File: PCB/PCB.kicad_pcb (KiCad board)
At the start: 2 copper layers, 31 parts, among them SW1 Bourns PEC11R, SW2 Bourns PEC11R, U1 RPi_Pico_TH, U2 RDA5807M_Module, U3 LM386, U4 AP63205WU-7

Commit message: PCB design #1
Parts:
- added ?: , , F.Cu at (179.0, 53.5)
- added LS1: Speaker, 2pin_ScrewTerminal:691137710002, F.Cu at (177.5, 76.5)
- added SW3: SW_DPST, 2pin_ScrewTerminal:691137710002, F.Cu at (156.5, 131.0)
- added SW4: SW_DPST, 2pin_ScrewTerminal:691137710002, F.Cu at (145.5, 131.0)
- added SW5: SW_DPST, 2pin_ScrewTerminal:691137710002, F.Cu at (134.5, 131.0)
- BT1: footprint Battery:BatteryHolder_Bulgin_BX0034_1xAAA -> Battery:THT Battery Connection
- SW1, SW2: footprint Rotary_Encoder:RotaryEncoder_Alps_EC12E-Switch_Vertical_H20mm -> 5pin_ScrewTerminal:PHOENIX_1935190
- moved U3 100.2 mm to (158.0, 79.0)
- moved R3 88.6 mm to (172.2, 84.0)
- moved U2 84.9 mm to (171.4, 63.5)
- moved BT1 78.1 mm to (128.2, 65.9)
- moved C1 72.4 mm to (164.5, 84.0)
- moved C2 70.0 mm to (164.5, 77.5)
- moved U1 69.9 mm to (141.1, 97.4)
- moved C10 69.9 mm to (131.2, 59.9)
- moved C11 69.9 mm to (131.2, 57.4)
- moved C8 69.9 mm to (132.8, 66.9)
- moved C9 69.9 mm to (135.8, 60.4)
- moved U4 69.9 mm to (133.2, 63.5)
- moved L1 69.9 mm to (137.4, 63.4)
- moved R2 68.2 mm to (152.7, 64.5)
- moved R1 68.1 mm to (152.7, 61.5)
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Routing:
- net /Encoder2SW: track 0.00 -> 66.0 mm
- net /B1: track 0.00 -> 46.7 mm
- net /Encoder2B: track 0.00 -> 42.6 mm
- net Net-(U1-VSYS): track 43.1 -> 0.61 mm
- net /Radio sdio: track 0.00 -> 41.1 mm
- net /Radio sclk: track 0.00 -> 40.9 mm
- net /B2: track 0.00 -> 39.3 mm
- net /Display CS: track 0.00 -> 37.1 mm
- net /Encoder1SW: track 0.00 -> 35.4 mm
- net /B3: track 0.00 -> 34.7 mm
- net Net-(U2-LOUT): track 0.00 -> 31.9 mm
- net /Encoder1A: track 0.00 -> 31.9 mm
- net /Display res: track 0.00 -> 25.8 mm
- net /Encoder2A: track 0.00 -> 23.5 mm
- net Net-(R4-Pad2): track 0.00 -> 21.4 mm
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- added copper zone on F.Cu, net 3V3
- added copper zone on B.Cu, net GND
- added copper zone on F.Cu, net GND
- added copper zone on F.Cu, net Net-(BT1-+)
- added copper zone on F.Cu, net Net-(U1-VSYS)
- added copper zone on F.Cu, net Net-(U4-SW)
- removed copper zone on F.Cu, net (none)
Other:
- board outline added: 83 x 95 mm

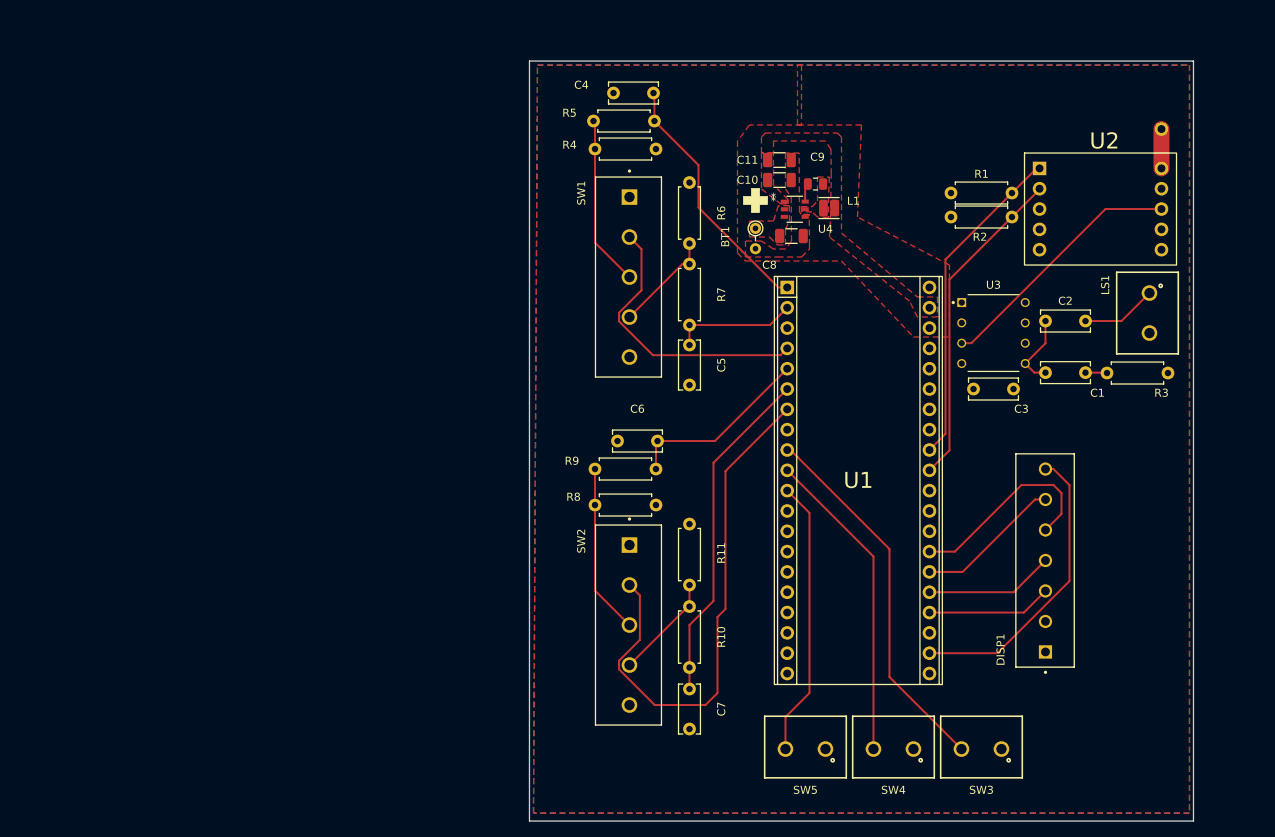
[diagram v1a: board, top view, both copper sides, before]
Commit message: Updated PCB
PCB updated to reflect new footprints and corrected connections.
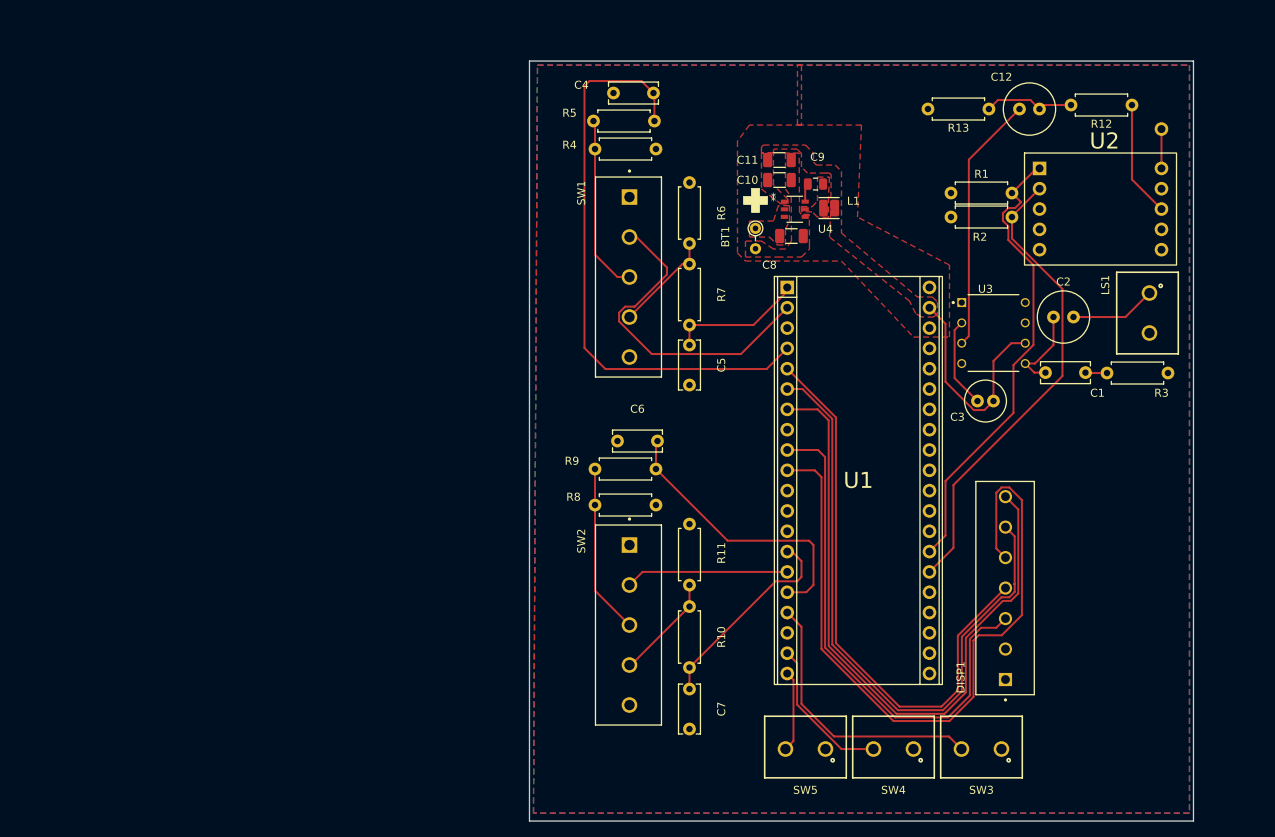
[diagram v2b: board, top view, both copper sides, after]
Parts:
- added C12: 470uF, Capacitor_THT:C_Radial_D6.3mm_H11.0mm_P2.50mm, F.Cu at (163.8, 51.0)
- added R12: 1k, Resistor_THT:R_Axial_DIN0207_L6.3mm_D2.5mm_P7.62mm_Horizontal, F.Cu at (175.3, 50.5)
- added R13: 150, Resistor_THT:R_Axial_DIN0207_L6.3mm_D2.5mm_P7.62mm_Horizontal, F.Cu at (157.4, 51.0)
- C2: footprint Capacitor_THT:C_Disc_D6.0mm_W2.5mm_P5.00mm -> Capacitor_THT:C_Radial_D6.3mm_H11.0mm_P2.50mm
- C3: value 470uF -> 10uF; footprint Capacitor_THT:C_Disc_D6.0mm_W2.5mm_P5.00mm -> Capacitor_THT:C_Radial_D5.0mm_H11.0mm_P2.00mm
- R3: value 10k -> 10
- moved DISP1 6.07 mm to (163.1, 124.2)
- moved C3 1.58 mm to (156.0, 87.5)
- moved C2 1.12 mm to (165.5, 77.0)
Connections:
- C10 pad 2: Net-(U1-VSYS) -> 5V
- C11 pad 2: Net-(U1-VSYS) -> 5V
- C3 pad 1: GND -> Net-(U3--)
- C3 pad 2: 3V3 -> 5V
- L1 pad 2: Net-(U1-VSYS) -> 5V
- SW1 pad C: unconnected-(SW1-PadC) -> GND
- SW2 pad C: unconnected-(SW2-PadC) -> GND
- U1 pad 1: /Encoder1A -> /Encoder1B
- U1 pad 10: /B2 -> /Display res
- U1 pad 11: /B3 -> unconnected-(U1-GP8-Pad11)
- U1 pad 14: unconnected-(U1-GP10-Pad14) -> /Encoder2B
- U1 pad 15: unconnected-(U1-GP11-Pad15) -> /Encoder2SW
- U1 pad 16: unconnected-(U1-GP12-Pad16) -> /Encoder2A
- U1 pad 17: unconnected-(U1-GP13-Pad17) -> /B1
- U1 pad 19: unconnected-(U1-GP14-Pad19) -> /B2
- U1 pad 2: /Encoder1B -> /Encoder1SW
- U1 pad 20: unconnected-(U1-GP15-Pad20) -> /B3
- U1 pad 22: /Display CS -> unconnected-(U1-GP17-Pad22)
- U1 pad 24: /Display sck -> unconnected-(U1-GP18-Pad24)
- U1 pad 25: /Display sda -> unconnected-(U1-GP19-Pad25)
- U1 pad 26: /Display DC -> /Radio sclk
- U1 pad 27: /Display res -> /Radio sdio
- U1 pad 31: /Radio sclk -> unconnected-(U1-GP26/ADC0-Pad31)
- U1 pad 32: /Radio sdio -> unconnected-(U1-GP27/ADC1-Pad32)
- U1 pad 39: Net-(U1-VSYS) -> 5V
- U1 pad 4: /Encoder1SW -> /Encoder1A
- U1 pad 5: /Encoder2A -> /Display sda
- U1 pad 6: /Encoder2B -> /Display DC
- U1 pad 7: /Encoder2SW -> /Display CS
- U1 pad 9: /B1 -> /Display sck
- U3 pad 2: GND -> Net-(U3--)
- U3 pad 3: Net-(U2-LOUT) -> Net-(U3-+)
- U3 pad 6: 3V3 -> 5V
- U4 pad 1: Net-(U1-VSYS) -> 5V
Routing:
- net /Display res: track 25.8 -> 91.6 mm
- net /Display DC: track 18.2 -> 80.3 mm
- net /Display sda: track 16.1 -> 71.4 mm
- net /Display sck: track 15.6 -> 64.3 mm
- net /Display CS: track 37.1 -> 84.2 mm
- net /Encoder2SW: track 66.0 -> 20.4 mm
- net /Encoder1A: track 31.9 -> 73.3 mm
- net Net-(U3-+): track 0.00 -> 32.3 mm
- net 5V: track 0.00 -> 27.9 mm
- net /B3: track 34.7 -> 10.2 mm
- net /B2: track 39.3 -> 18.8 mm
- net /Radio sclk: track 40.9 -> 58.8 mm
- net Net-(U2-LOUT): track 31.9 -> 14.5 mm
- net /Radio sdio: track 41.1 -> 58.4 mm
- net /Encoder2B: track 42.6 -> 25.6 mm
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- added copper zone on F.Cu, net 5V
- removed copper zone on F.Cu, net Net-(U1-VSYS)

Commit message: Updated PCB
PCB updated to have mounting holes, proper shape, etc.
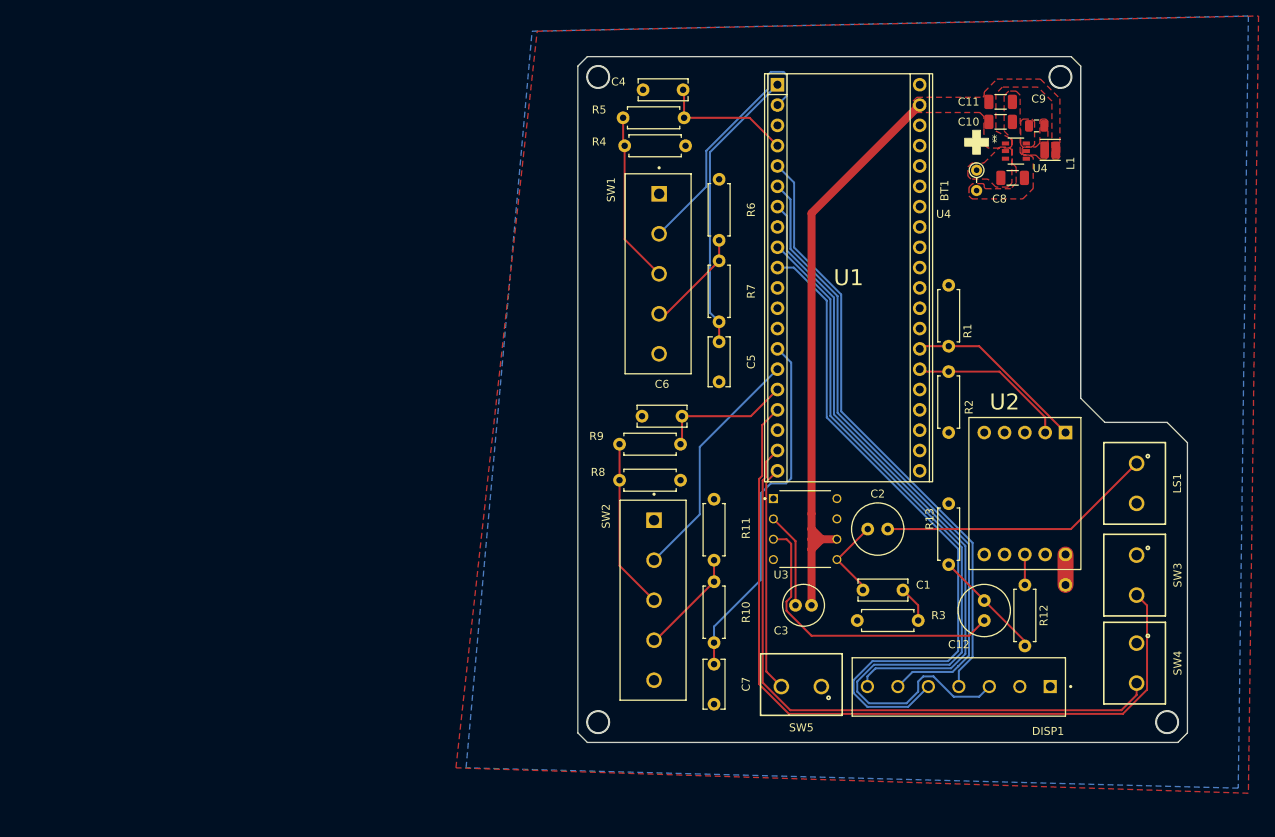
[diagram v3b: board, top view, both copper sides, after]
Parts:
- moved C12 61.8 mm to (156.8, 112.4), turned to -90 degrees
- moved R12 61.5 mm to (161.9, 110.5), turned to -90 degrees
- moved ? 58.2 mm to (167.0, 110.5)
- moved R13 57.2 mm to (152.4, 108.0), turned to 90 degrees
- moved R3 38.9 mm to (148.6, 114.9), turned to 180 degrees
- moved U2 36.8 mm to (161.9, 99.1), turned to -90 degrees
- moved C1 35.5 mm to (141.7, 111.1)
- moved C2 35.2 mm to (142.3, 103.5)
- moved C3 34.2 mm to (133.3, 113.0)
- moved U3 34.0 mm to (134.5, 103.5)
- moved SW4 32.2 mm to (175.9, 120.3), turned to -90 degrees
- moved SW3 29.1 mm to (175.9, 109.3), turned to -90 degrees
- moved BT1 28.6 mm to (155.9, 58.6)
- moved C10 28.6 mm to (158.9, 52.6)
- moved C11 28.6 mm to (158.9, 50.1)
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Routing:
- net /B1: track 35.3 -> 98.9 mm
- net /B2: track 18.8 -> 80.2 mm
- net /Encoder1A: track 73.3 -> 16.7 mm
- net 5V: track 27.9 -> 74.9 mm
- net /Radio sclk: track 58.8 -> 20.1 mm
- net /Radio sdio: track 58.4 -> 22.8 mm
- net /Display sck: track 64.3 -> 96.9 mm
- net Net-(C2-Pad2): track 10.7 -> 34.5 mm
- net /Encoder2B: track 25.6 -> 45.2 mm
- net /Encoder1B: track 16.9 -> 36.1 mm
- net /Encoder2A: track 35.9 -> 16.9 mm
- net /B3: track 10.2 -> 28.3 mm
- net Net-(U2-LOUT): track 14.5 -> 3.81 mm
- net /Encoder2SW: track 20.4 -> 30.3 mm
- net /Encoder1SW: track 41.8 -> 32.4 mm
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- added copper zone on F.Cu, net Net-(U4-BST)
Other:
- board size 83 x 95 mm -> 76.2 x 85.7 mm
- board text added: "U4"

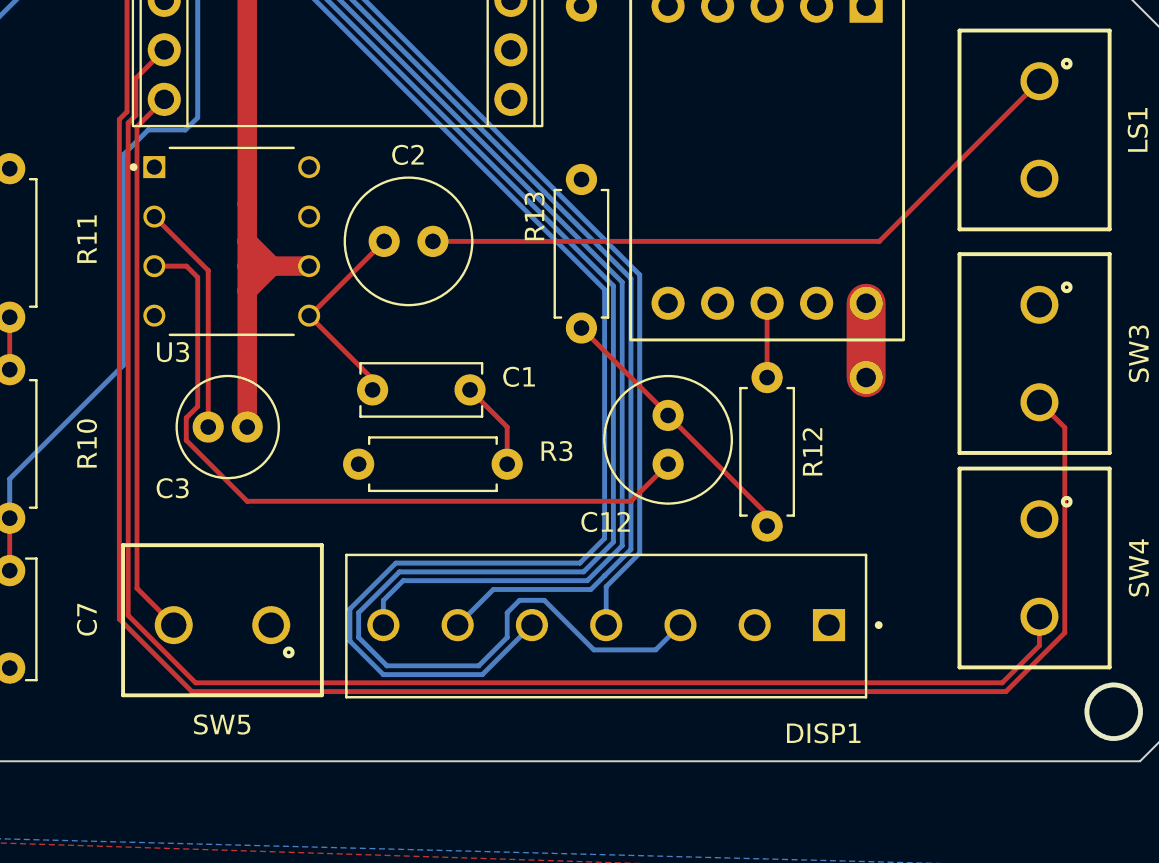
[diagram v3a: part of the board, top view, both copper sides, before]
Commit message: Updated SW5 footprint
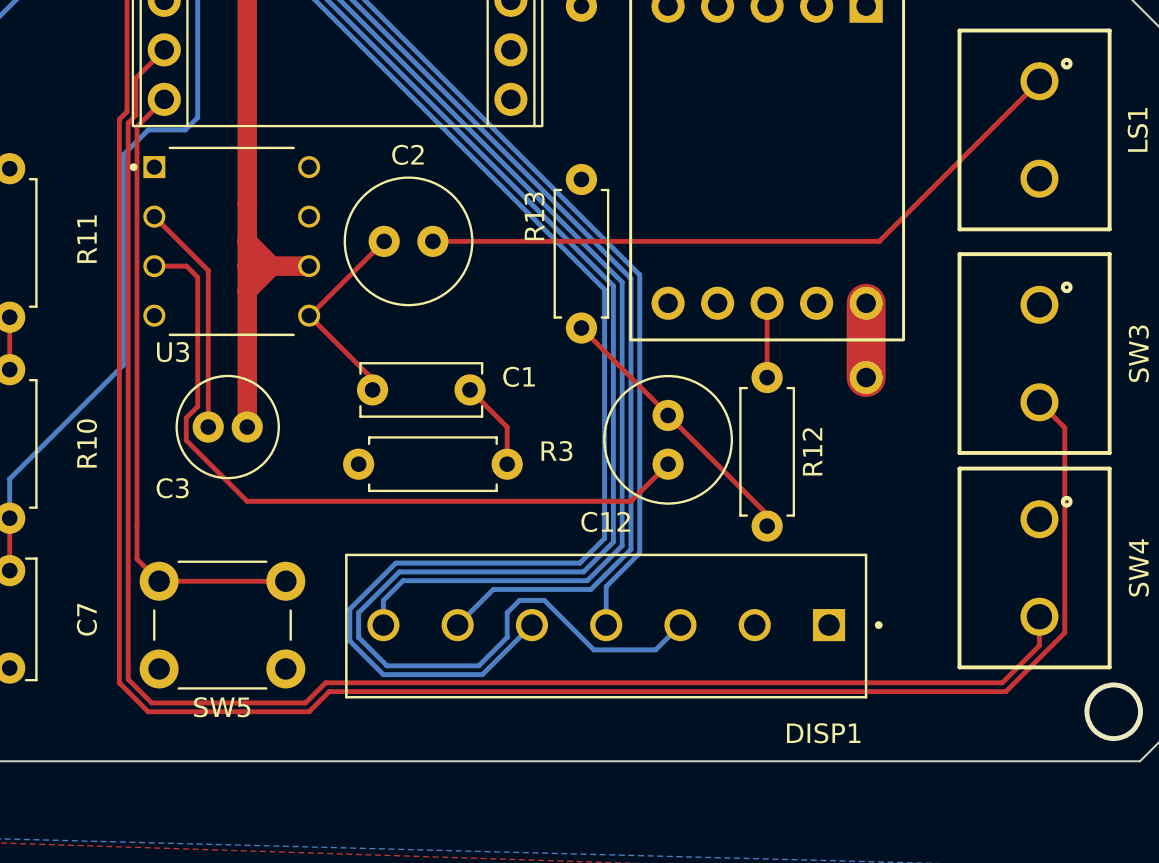
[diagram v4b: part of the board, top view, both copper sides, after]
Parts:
- SW5: footprint 2pin_ScrewTerminal:691137710002 -> Button_Switch_THT:SW_PUSH_6mm_H7.3mm
- moved SW5 3.95 mm to (137.2, 125.4)
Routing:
- net /B3: track 28.3 -> 32.3 mm
- net /B2: track 80.2 -> 83.0 mm
- net /B1: track 98.9 -> 101.7 mm
